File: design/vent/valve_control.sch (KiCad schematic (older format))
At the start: 26 parts, among them J14 Conn_01x03, J15 Conn_01x03, Q3 AOD417, Q4 AOD417, Q5 DMG2302UK, Q6 DMG2302UK, Q7 AOD476, Q8 AOD476

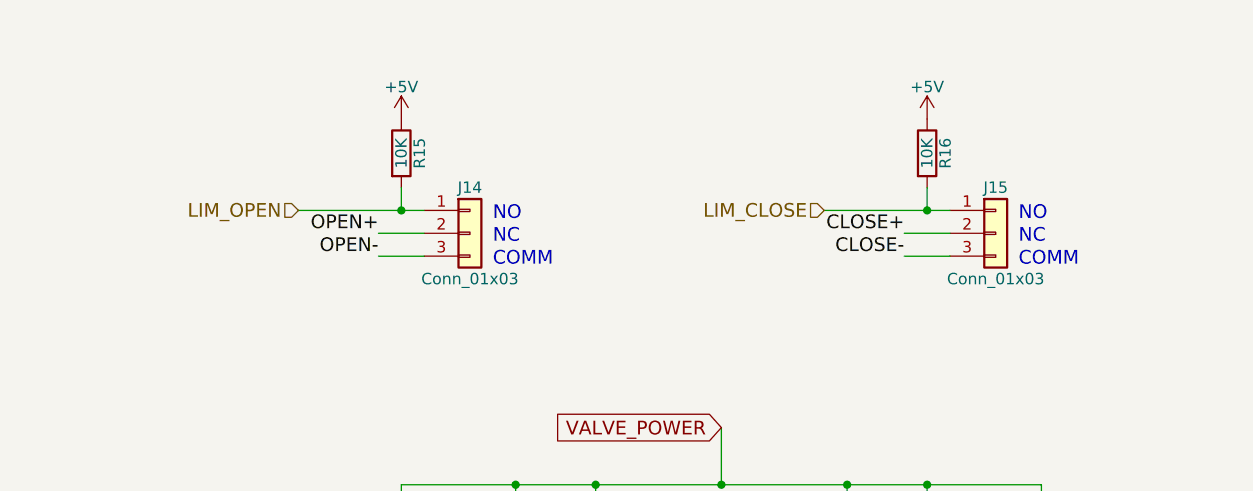
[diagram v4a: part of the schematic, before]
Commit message: Add connector part numbers to schematic
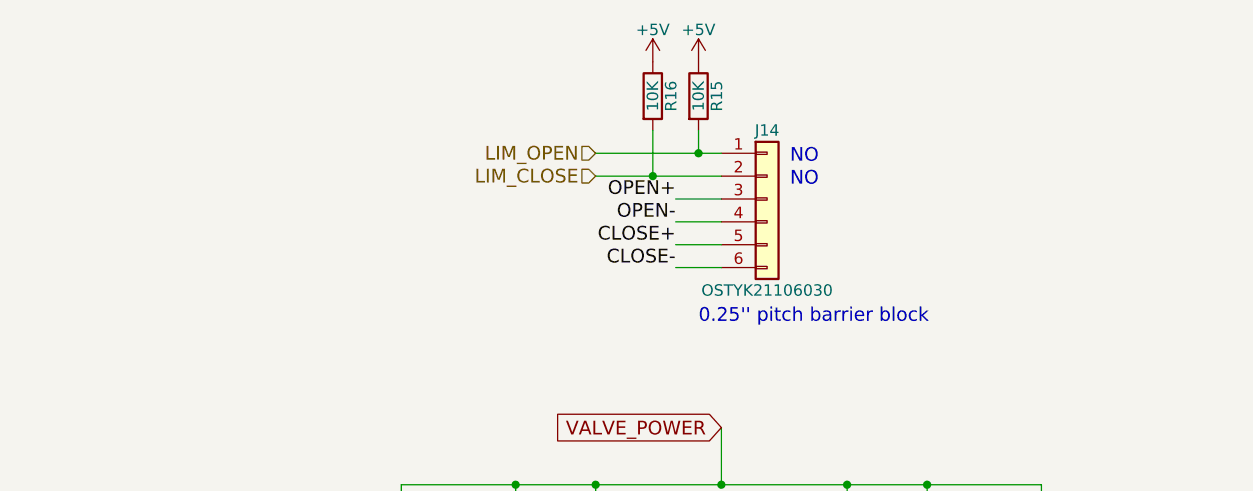
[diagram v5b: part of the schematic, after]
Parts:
- removed J14, J15: Conn_01x03, symbol Conn_01x03
- added J14: OSTYK21106030, symbol Conn_01x06
- Q3, Q4, Q7, Q8: footprint (none) -> TO_SOT_Packages_SMD:TO-252-2
- Q5, Q6: footprint (none) -> TO_SOT_Packages_SMD:SOT-23_Handsoldering
- R15, R16, R17, R18, R19, R20, R21, R22, R23, R24, R25, R26, R31, R32: footprint (none) -> Resistors_SMD:R_0805_HandSoldering
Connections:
- net CLOSE+: now also J14.5 (Pin_5)
- net CLOSE-: now also J14.6 (Pin_6)
- net LIM_CLOSE: now also J14.2 (Pin_2)
- net LIM_OPEN: now also J14.1 (Pin_1)
- net OPEN+: now also J14.3 (Pin_3)
- net OPEN-: now also J14.4 (Pin_4)
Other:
- note added: "0.25'' pitch barrier block"
- note removed: "COMM"
- note removed: "NC"
- moved on the sheet: R15, R16

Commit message: Add barrier block footprints
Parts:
- J14: footprint (none) -> Flight_Instr:Barrier_Strip_6Circuit
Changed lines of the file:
@@
 F 0 "J14" H 5800 2500 50  0000 C CNN
 F 1 "OSTYK21106030" H 5800 1800 50  0000 C CNN
-F 2 "" H 5800 2200 50  0001 C CNN
+F 2 "Flight_Instr:Barrier_Strip_6Circuit" H 5800 2200 50  0001 C CNN
 F 3 "" H 5800 2200 50  0001 C CNN
 	1    5800 2200

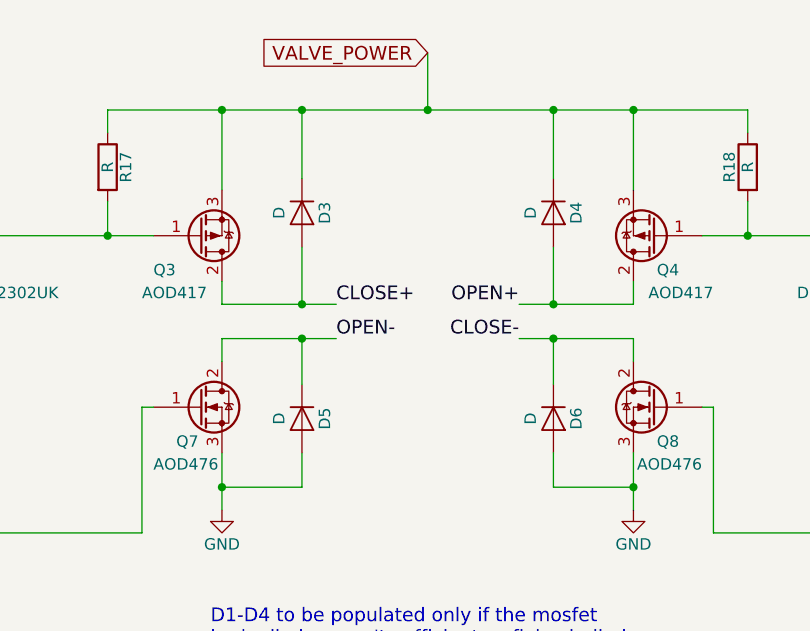
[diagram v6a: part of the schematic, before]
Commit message: Add more part numbers and footprints
- Flyback diodes
- Fuses
- Xbee
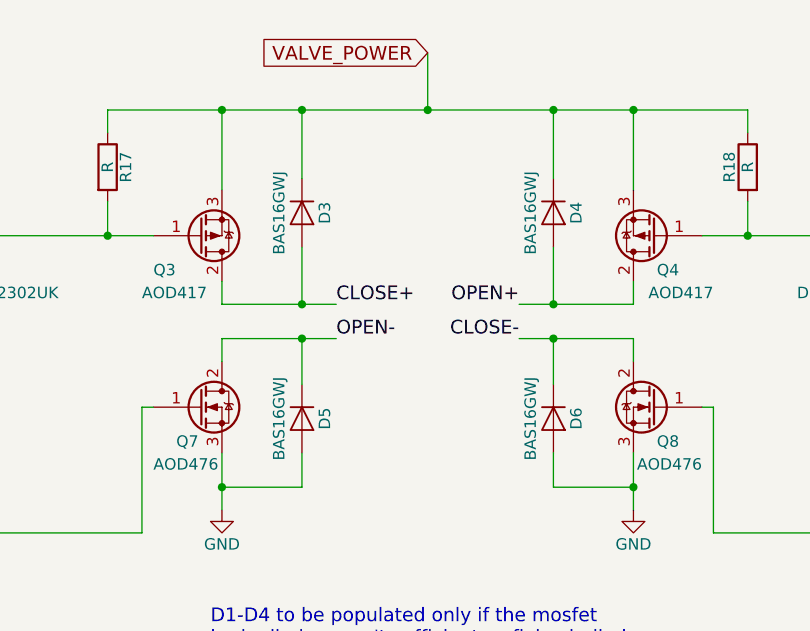
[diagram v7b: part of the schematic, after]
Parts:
- D3, D4, D5, D6: value D -> BAS16GWJ; footprint (none) -> Flight_Instr:D_SOD-123_HandSoldering
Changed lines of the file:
@@
 $EndDescr
 $Comp
-L GND #PWR075
+L GND #PWR073
 U 1 1 5AE16382
 P 4700 5200
-F 0 "#PWR075" H 4700 4950 50  0001 C CNN
+F 0 "#PWR073" H 4700 4950 50  0001 C CNN
 F 1 "GND" H 4700 5050 50  0000 C CNN
 F 2 "" H 4700 5200 50  0001 C CNN
@@
 $EndComp
 $Comp
-L GND #PWR076
+L GND #PWR074
 U 1 1 5AE163E6
 P 6500 5200
-F 0 "#PWR076" H 6500 4950 50  0001 C CNN
+F 0 "#PWR074" H 6500 4950 50  0001 C CNN
 F 1 "GND" H 6500 5050 50  0000 C CNN
 F 2 "" H 6500 5200 50  0001 C CNN
@@
 $EndComp
 $Comp
-L GND #PWR077
+L GND #PWR075
 U 1 1 5AE172FE
 P 3450 4500
-F 0 "#PWR077" H 3450 4250 50  0001 C CNN
+F 0 "#PWR075" H 3450 4250 50  0001 C CNN
 F 1 "GND" H 3450 4350 50  0000 C CNN
 F 2 "" H 3450 4500 50  0001 C CNN
@@
 $EndComp
 $Comp
-L +5V #PWR078
+L +5V #PWR076
 U 1 1 5AE4C96A
 P 5500 1600
-F 0 "#PWR078" H 5500 1450 50  0001 C CNN
+F 0 "#PWR076" H 5500 1450 50  0001 C CNN
 F 1 "+5V" H 5500 1740 50  0000 C CNN
 F 2 "" H 5500 1600 50  0001 C CNN
@@
 $EndComp
 $Comp
-L +5V #PWR079
+L +5V #PWR077
 U 1 1 5AE4D097
 P 5300 1600
-F 0 "#PWR079" H 5300 1450 50  0001 C CNN
+F 0 "#PWR077" H 5300 1450 50  0001 C CNN
 F 1 "+5V" H 5300 1740 50  0000 C CNN
 F 2 "" H 5300 1600 50  0001 C CNN
@@
 $EndComp
 $Comp
-L GND #PWR080
+L GND #PWR078
 U 1 1 5AEBE82B
 P 3100 4500
-F 0 "#PWR080" H 3100 4250 50  0001 C CNN
+F 0 "#PWR078" H 3100 4250 50  0001 C CNN
 F 1 "GND" H 3100 4350 50  0000 C CNN
 F 2 "" H 3100 4500 50  0001 C CNN
@@
 $EndComp
 $Comp
-L +5V #PWR081
+L +5V #PWR079
 U 1 1 5AEBF207
 P 3100 5000
-F 0 "#PWR081" H 3100 4850 50  0001 C CNN
+F 0 "#PWR079" H 3100 4850 50  0001 C CNN
 F 1 "+5V" H 3100 5140 50  0000 C CNN
 F 2 "" H 3100 5000 50  0001 C CNN
@@
 $EndComp
 $Comp
-L GND #PWR082
+L GND #PWR080
 U 1 1 5AEBFD20
 P 7750 4500
-F 0 "#PWR082" H 7750 4250 50  0001 C CNN
+F 0 "#PWR080" H 7750 4250 50  0001 C CNN
 F 1 "GND" H 7750 4350 50  0000 C CNN
 F 2 "" H 7750 4500 50  0001 C CNN
@@
 $EndComp
 $Comp
-L GND #PWR083
+L GND #PWR081
 U 1 1 5AEBFD35
 P 8100 5600
-F 0 "#PWR083" H 8100 5350 50  0001 C CNN
+F 0 "#PWR081" H 8100 5350 50  0001 C CNN
 F 1 "GND" H 8100 5450 50  0000 C CNN
 F 2 "" H 8100 5600 50  0001 C CNN
@@
 LOW_SIDE_B
 $Comp
-L +5V #PWR084
+L +5V #PWR082
 U 1 1 5AEBFD4A
 P 8100 3900
-F 0 "#PWR084" H 8100 3750 50  0001 C CNN
+F 0 "#PWR082" H 8100 3750 50  0001 C CNN
 F 1 "+5V" H 8100 4040 50  0000 C CNN
 F 2 "" H 8100 3900 50  0001 C CNN
@@
 P 5050 4800
 F 0 "D5" H 5050 4900 50  0000 C CNN
-F 1 "D" H 5050 4700 50  0000 C CNN
-F 2 "" H 5050 4800 50  0001 C CNN
+F 1 "BAS16GWJ" H 5050 4700 50  0000 C CNN
+F 2 "Flight_Instr:D_SOD-123_HandSoldering" H 5050 4800 50  0001 C CNN
 F 3 "" H 5050 4800 50  0001 C CNN
 	1    5050 4800
@@
 P 6150 4800
 F 0 "D6" H 6150 4900 50  0000 C CNN
-F 1 "D" H 6150 4700 50  0000 C CNN
-F 2 "" H 6150 4800 50  0001 C CNN
+F 1 "BAS16GWJ" H 6150 4700 50  0000 C CNN
+F 2 "Flight_Instr:D_SOD-123_HandSoldering" H 6150 4800 50  0001 C CNN
 F 3 "" H 6150 4800 50  0001 C CNN
 	1    6150 4800
@@
 P 5050 3900
 F 0 "D3" H 5050 4000 50  0000 C CNN
-F 1 "D" H 5050 3800 50  0000 C CNN
-F 2 "" H 5050 3900 50  0001 C CNN
+F 1 "BAS16GWJ" H 5050 3800 50  0000 C CNN
+F 2 "Flight_Instr:D_SOD-123_HandSoldering" H 5050 3900 50  0001 C CNN
 F 3 "" H 5050 3900 50  0001 C CNN
 	1    5050 3900
@@
 P 6150 3900
 F 0 "D4" H 6150 4000 50  0000 C CNN
-F 1 "D" H 6150 3800 50  0000 C CNN
-F 2 "" H 6150 3900 50  0001 C CNN
+F 1 "BAS16GWJ" H 6150 3800 50  0000 C CNN
+F 2 "Flight_Instr:D_SOD-123_HandSoldering" H 6150 3900 50  0001 C CNN
 F 3 "" H 6150 3900 50  0001 C CNN
 	1    6150 3900
@@
 $EndComp
 $Comp
-L +5V #PWR085
+L +5V #PWR083
 U 1 1 5AF107D5
 P 3000 3900
-F 0 "#PWR085" H 3000 3750 50  0001 C CNN
+F 0 "#PWR083" H 3000 3750 50  0001 C CNN
 F 1 "+5V" H 3000 4040 50  0000 C CNN
 F 2 "" H 3000 3900 50  0001 C CNN
@@
 $EndComp
 $Comp
-L GND #PWR086
+L GND #PWR084
 U 1 1 5AF10AEB
 P 3000 5650
-F 0 "#PWR086" H 3000 5400 50  0001 C CNN
+F 0 "#PWR084" H 3000 5400 50  0001 C CNN
 F 1 "GND" H 3000 5500 50  0000 C CNN
 F 2 "" H 3000 5650 50  0001 C CNN
